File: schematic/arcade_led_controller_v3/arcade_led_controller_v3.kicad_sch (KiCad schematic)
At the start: 63 parts, among them J1 GND_BUS_1, J2 GND_BUS_2, J3 PSU_GND_BUS, P1_BALLTOP_LED_1 WS2812B, P1_BUTTONS_LED1 WS2812B, P1_DP_JOY_MODE_LED1 LED, P1_JOYSTICK_LED1 WS2812B, P1_LS_JOY_MODE_LED1 LED, P1_RS_JOY_MODE_LED1 LED, P2_BALLTOP_LED_1 WS2812B, P2_BUTTONS_LED1 WS2812B, P2_DP_JOY_MODE_LED1 LED, P2_JOYSTICK_LED1 WS2812B, P2_LS_JOY_MODE_LED1 LED, P2_RS_JOY_MODE_LED1 LED, Q1 Q_NMOS_GDS, Q2 Q_NMOS_GDS, Q3 Q_NMOS_GDS, Q4(PN2222)1 PN2222A, Q5(PN222)1 PN2222A, Q6(PN2222)1 PN2222A, Q7(PN2222)1 PN2222A, SW1 RotaryEncoder_Switch, U1 74AHCT125, U2 74AHCT125, U3 EA_DOGL128X-6

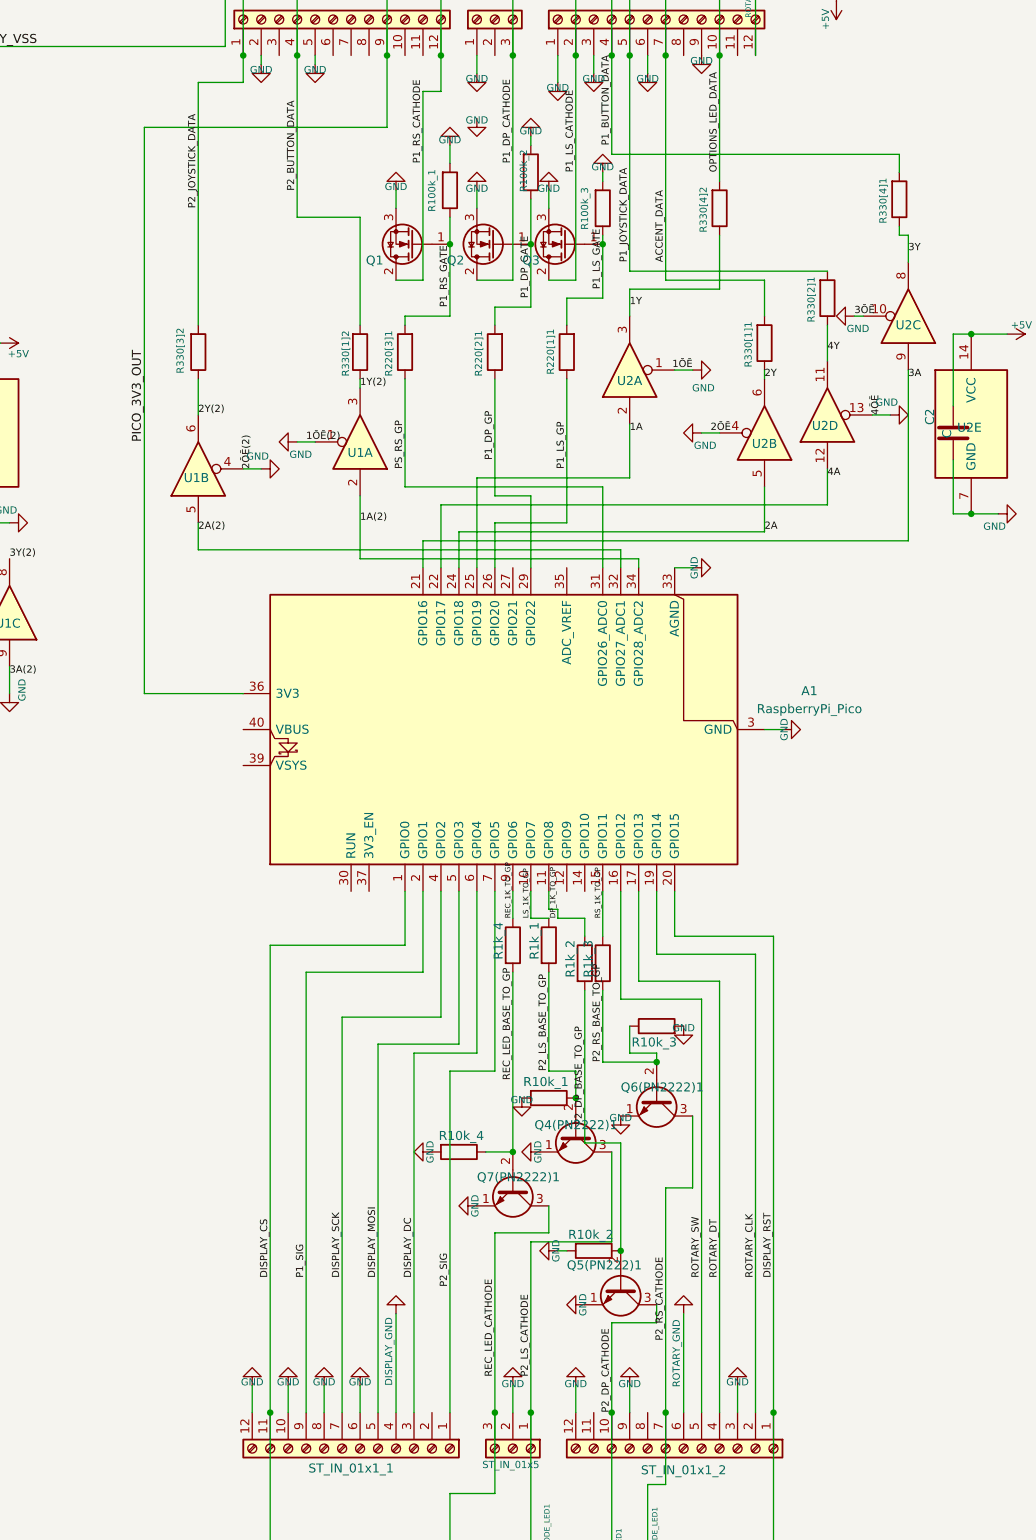
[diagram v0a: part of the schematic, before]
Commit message: replace pico footprint with 1x20 pin header sockets
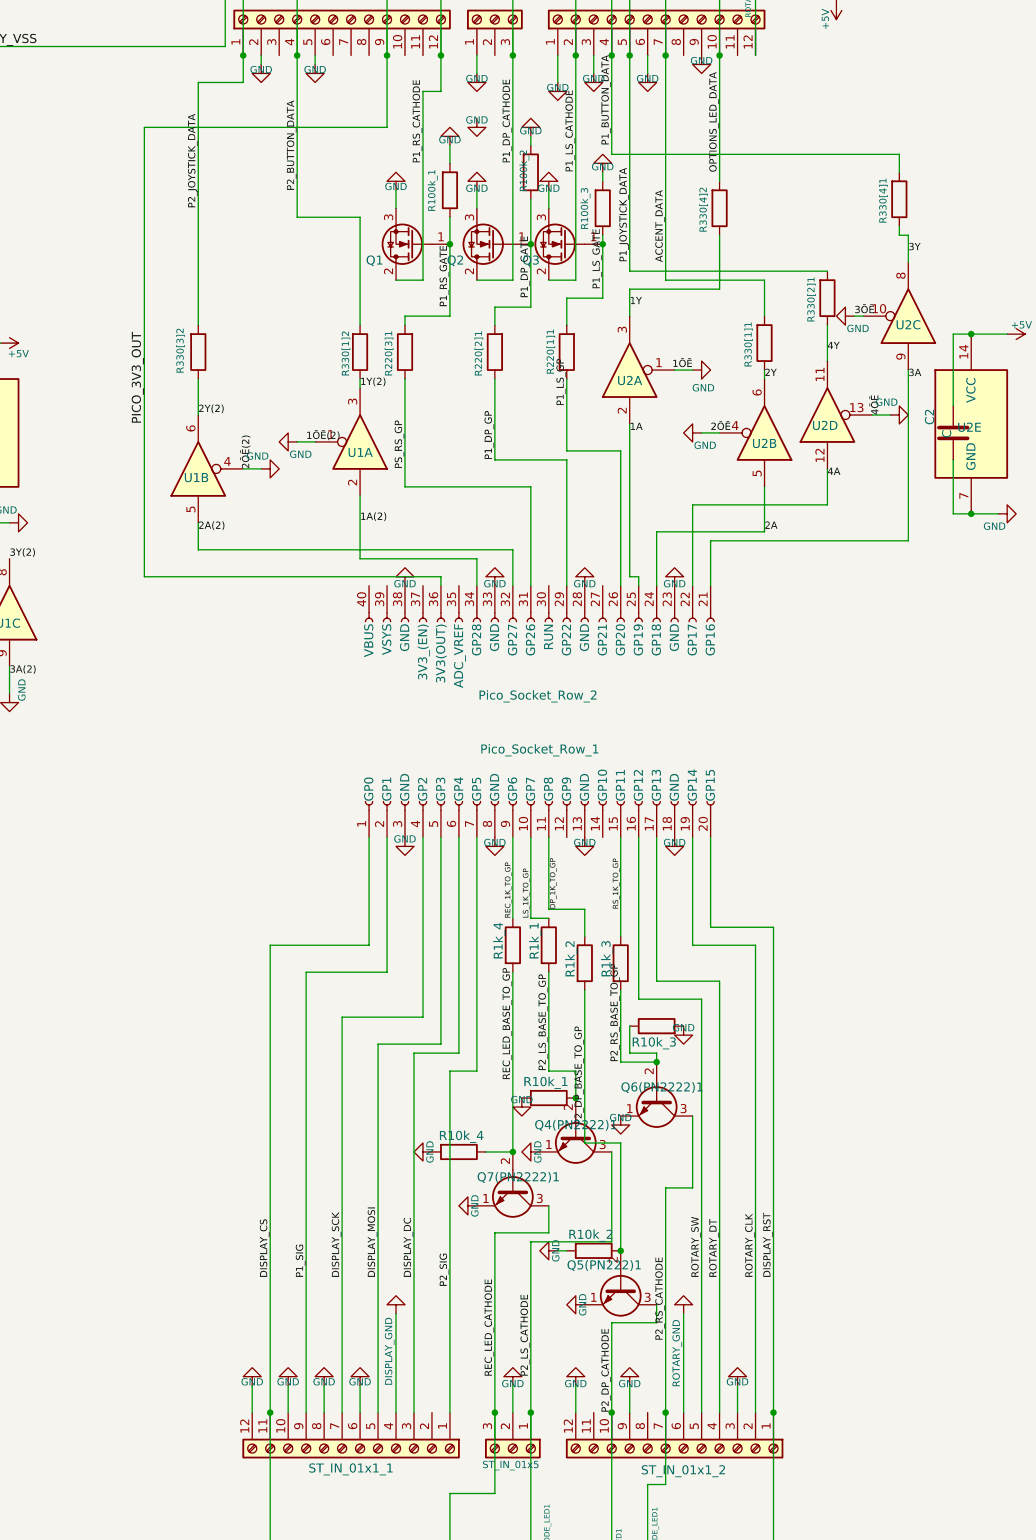
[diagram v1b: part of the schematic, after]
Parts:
- removed A1: RaspberryPi_Pico, Module:RaspberryPi_Pico_Common_THT, symbol MCU_Module:RaspberryPi_Pico
- added J4: Pico_Socket_Row_2, Connector_PinSocket_2.54mm:PinSocket_1x20_P2.54mm_Vertical, symbol Connector:Conn_01x20_Socket
- added J5: Pico_Socket_Row_1, Connector_PinSocket_2.54mm:PinSocket_1x20_P2.54mm_Vertical, symbol Connector:Conn_01x20_Socket
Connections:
- net 1A: now also J4.25 (GP19)
- net 1A(2): now also J4.34 (GP28)
- net 2A: now also J4.24 (GP18)
- net 2A(2): now also J4.32 (GP27)
- net 3A: now also J4.21 (GP16)
- net 4A: now also J4.22 (GP17)
- net DISPLAY_CS: now also J5.1 (GP0)
- net DISPLAY_DC: now also J5.6 (GP4)
- net DISPLAY_MOSI: now also J5.5 (GP3)
- net DISPLAY_RST: now also J5.20 (GP15)
- net DISPLAY_SCK: now also J5.4 (GP2)
- net DISPLAY_VSS: now also J4.36 (3V3(OUT))
- net DP_1K_TO_GP: now also J5.11 (GP8)
- net GND: now also J4.23 (GND), J4.28 (GND), J4.33 (GND), J4.38 (GND), J5.13 (GND), J5.18 (GND), J5.3 (GND), J5.8 (GND)
- net LS_1K_TO_GP: now also J5.10 (GP7)
- net P1_DP_GP: now also J4.29 (GP22)
- net P1_LS_GP: now also J4.26 (GP20)
- net P1_SIG: now also J5.2 (GP1)
- net P2_SIG: now also J5.7 (GP5)
- net PS_RS_GP: now also J4.31 (GP26)
- net REC_1K_TO_GP: now also J5.9 (GP6)
- net ROTARY_CLK: now also J5.19 (GP14)
- net ROTARY_DT: now also J5.17 (GP13)
- net ROTARY_SW: now also J5.16 (GP12)
- net RS_1K_TO_GP: now also J5.15 (GP11)
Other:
- moved on the sheet: R1k_3

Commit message: Update tracks
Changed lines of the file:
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@@
 	(wire
 		(pts
-			(xy 189.23 67.31) (xy 189.23 72.39)
+			(xy 180.34 78.74) (xy 165.1 78.74)
 		)
 		(stroke
@@
 	(wire
 		(pts
+			(xy 200.66 82.55) (xy 172.72 82.55)
+		)
+		(stroke
+			(width 0)
+			(type default)
+		)
+	)
+	(wire
+		(pts
 			(xy 134.62 148.59) (xy 125.73 148.59)
 		)
@@
 	(wire
 		(pts
-			(xy 165.1 76.2) (xy 165.1 83.82)
-		)
-		(stroke
-			(width 0)
-			(type default)
-		)
-	)
-	(wire
-		(pts
 			(xy 137.16 119.38) (xy 137.16 149.86)
 		)
@@
 	(wire
 		(pts
-			(xy 170.18 72.39) (xy 170.18 83.82)
-		)
-		(stroke
-			(width 0)
-			(type default)
-		)
-	)
-	(wire
-		(pts
 			(xy 149.86 175.26) (xy 149.86 171.45)
 		)
@@
 	(wire
 		(pts
+			(xy 189.23 67.31) (xy 189.23 81.28)
+		)
+		(stroke
+			(width 0)
+			(type default)
+		)
+	)
+	(wire
+		(pts
 			(xy 165.1 119.38) (xy 165.1 139.7)
 		)
@@
 	(wire
 		(pts
-			(xy 180.34 69.85) (xy 180.34 76.2)
-		)
-		(stroke
-			(width 0)
-			(type default)
-		)
-	)
-	(wire
-		(pts
 			(xy 135.89 152.4) (xy 135.89 200.66)
 		)
@@
 	(wire
 		(pts
-			(xy 200.66 53.34) (xy 200.66 77.47)
-		)
-		(stroke
-			(width 0)
-			(type default)
-		)
-	)
-	(wire
-		(pts
 			(xy 170.18 158.75) (xy 170.18 168.91)
 		)
@@
 	(wire
 		(pts
-			(xy 172.72 77.47) (xy 172.72 83.82)
+			(xy 170.18 81.28) (xy 170.18 83.82)
 		)
 		(stroke
@@
 	(wire
 		(pts
+			(xy 172.72 82.55) (xy 172.72 83.82)
+		)
+		(stroke
+			(width 0)
+			(type default)
+		)
+	)
+	(wire
+		(pts
 			(xy 161.29 -41.91) (xy 161.29 8.89)
 		)
@@
 	(wire
 		(pts
-			(xy 180.34 76.2) (xy 165.1 76.2)
-		)
-		(stroke
-			(width 0)
-			(type default)
-		)
-	)
-	(wire
-		(pts
 			(xy 199.39 34.29) (xy 199.39 33.02)
 		)
@@
 	(wire
 		(pts
+			(xy 180.34 69.85) (xy 180.34 78.74)
+		)
+		(stroke
+			(width 0)
+			(type default)
+		)
+	)
+	(wire
+		(pts
 			(xy 73.66 -71.12) (xy 87.63 -71.12)
 		)
@@
 	(wire
 		(pts
+			(xy 200.66 53.34) (xy 200.66 82.55)
+		)
+		(stroke
+			(width 0)
+			(type default)
+		)
+	)
+	(wire
+		(pts
 			(xy 158.75 8.89) (xy 158.75 22.86)
 		)
@@
 	(wire
 		(pts
-			(xy 189.23 72.39) (xy 170.18 72.39)
-		)
-		(stroke
-			(width 0)
-			(type default)
-		)
-	)
-	(wire
-		(pts
 			(xy 113.03 196.85) (xy 113.03 200.66)
 		)
@@
 	(wire
 		(pts
+			(xy 189.23 81.28) (xy 170.18 81.28)
+		)
+		(stroke
+			(width 0)
+			(type default)
+		)
+	)
+	(wire
+		(pts
 			(xy 137.16 -41.91) (xy 137.16 -38.1)
 		)
@@
 	(wire
 		(pts
-			(xy 200.66 77.47) (xy 172.72 77.47)
-		)
-		(stroke
-			(width 0)
-			(type default)
-		)
-	)
-	(wire
-		(pts
 			(xy 140.97 163.83) (xy 144.78 163.83)
 		)
@@
 		)
 		(stroke
+			(width 0)
+			(type default)
+		)
+	)
+	(wire
+		(pts
+			(xy 165.1 78.74) (xy 165.1 83.82)
+		)
+		(stroke

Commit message: More routing updates
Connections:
- net ACCENT_DATA: now also ST_OUT_01x12_2.8 (Pin_8); no longer ACCENT_LED1.4 (DIN), ST_OUT_01x12_2.7 (Pin_7)
- net DISPLAY_VSS: now also ST_OUT_01x12_1.7 (Pin_7); no longer ST_OUT_01x12_1.9 (Pin_9)
- net GND: now also ST_OUT_01x12_1.9 (Pin_9), ST_OUT_01x12_2.5 (Pin_5), ST_OUT_01x12_2.7 (Pin_7); no longer ST_OUT_01x12_2.3 (Pin_3), ST_OUT_01x12_2.6 (Pin_6)
- net OPTIONS_LED_DATA: now also ST_OUT_01x12_2.6 (Pin_6); no longer OPTIONS_BUTTONS_LED1.3 (DIN), ST_OUT_01x12_2.10 (Pin_10)
- net P1_BUTTON_DATA: now also ST_OUT_01x12_2.10 (Pin_10); no longer P1_BUTTONS_LED1.3 (DIN), ST_OUT_01x12_2.4 (Pin_4)
- net P1_JOYSTICK_DATA: now also ST_OUT_01x12_2.11 (Pin_11); no longer P1_JOYSTICK_LED1.3 (DIN), ST_OUT_01x12_2.5 (Pin_5)
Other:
- moved on the sheet: R330[4]1, R330[4]2
